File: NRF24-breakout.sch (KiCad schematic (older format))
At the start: 2 parts, among them J1 CONN_01X08, U1 nRF24

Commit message: Wiring
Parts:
- U1: symbol nRF24 -> nRF24-RESCUE-NRF24-breakout
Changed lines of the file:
@@
 EESchema Schematic File Version 2
+LIBS:NRF24-breakout-rescue
 LIBS:power
 LIBS:device
@@
 $EndComp
 $Comp
-L nRF24 U1
+L nRF24-RESCUE-NRF24-breakout U1
 U 1 1 5971E2DB
 P 5400 3350

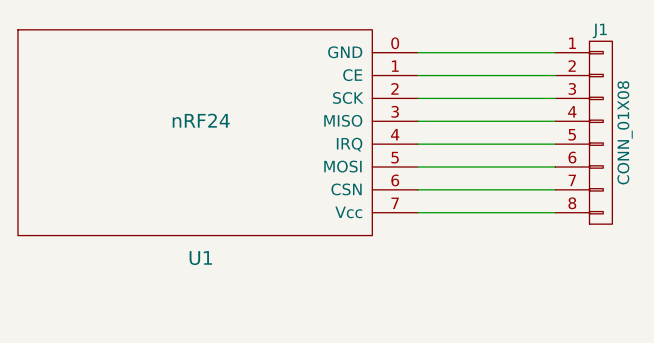
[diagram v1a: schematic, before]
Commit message: Add a capacitor to the schematic in Eeschema
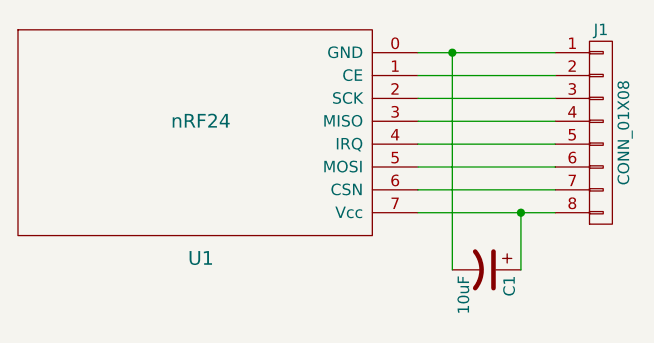
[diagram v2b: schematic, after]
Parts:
- added C1: 10uF, Capacitors_THT:CP_Radial_D10.0mm_P5.00mm, symbol CP1
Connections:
- net at J1.1 (P1), U1.0 (GND): now also C1.2
- net at J1.8 (P8), U1.7 (Vcc): now also C1.1
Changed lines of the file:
@@
 Wire Wire Line
 	6350 3750 6950 3750
+$Comp
+L CP1 C1
+U 1 1 598DE981
+P 6650 4000
+F 0 "C1" H 6675 4100 50  0000 L CNN
+F 1 "10uF" H 6675 3900 50  0000 L CNN
+F 2 "Capacitors_THT:CP_Radial_D10.0mm_P5.00mm" H 6650 4000 50  0001 C CNN
+F 3 "" H 6650 4000 50  0001 C CNN
+	1    6650 4000
+	0    1    1    0
+$EndComp
+Wire Wire Line
+	6500 4000 6500 3050
+Connection ~ 6500 3050
+Wire Wire Line
+	6800 4000 6800 3750
+Connection ~ 6800 3750
 $EndSCHEMATC
